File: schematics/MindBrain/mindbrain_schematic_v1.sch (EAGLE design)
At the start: 42 parts, among them IC1 TL084P, IC2 TL084P

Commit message: created board files in Eagle, started layout
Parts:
- added C1, C2, C3, C4: (no value), SparkFun-Capacitors:CAPKIT
- added CON1: POWER, SparkFun-Connectors:M05X2SHD
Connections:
- new net N$25: CON1.3, CON1.4, CON1.5, CON1.6, CON1.7, CON1.8
- new net N$27: CON1.1, CON1.2
- new net N$28: CON1.10, CON1.9
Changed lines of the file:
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@@
 <part name="GND16" library="SparkFun-Aesthetics" deviceset="GND" device=""/>
 <part name="IC2" library="linear" deviceset="TL084" device="P"/>
+<part name="C1" library="SparkFun-Capacitors" deviceset="CAP" device="KIT"/>
+<part name="C2" library="SparkFun-Capacitors" deviceset="CAP" device="KIT"/>
+<part name="C3" library="SparkFun-Capacitors" deviceset="CAP" device="KIT"/>
+<part name="C4" library="SparkFun-Capacitors" deviceset="CAP" device="KIT"/>
+<part name="CON1" library="SparkFun-Connectors" deviceset="M05X2" device="SHD" value="POWER"/>
 </parts>
 <sheets>
@@
 <instance part="IC2" gate="C" x="88.9" y="7.62"/>
 <instance part="IC2" gate="D" x="88.9" y="-30.48"/>
+<instance part="C1" gate="G$1" x="-55.88" y="53.34"/>
+<instance part="C2" gate="G$1" x="-45.72" y="53.34"/>
+<instance part="C3" gate="G$1" x="-55.88" y="40.64"/>
+<instance part="C4" gate="G$1" x="-45.72" y="40.64"/>
+<instance part="CON1" gate="G$1" x="-45.72" y="81.28"/>
 </instances>
 <busses>
@@
 </segment>
 </net>
+<net name="N$25" class="0">
+<segment>
+<pinref part="CON1" gate="G$1" pin="3"/>
+<pinref part="CON1" gate="G$1" pin="5"/>
+<wire x1="-53.34" y1="83.82" x2="-53.34" y2="81.28" width="0.1524" layer="91"/>
+<pinref part="CON1" gate="G$1" pin="7"/>
+<wire x1="-53.34" y1="81.28" x2="-53.34" y2="78.74" width="0.1524" layer="91"/>
+<wire x1="-53.34" y1="81.28" x2="-58.42" y2="81.28" width="0.1524" layer="91"/>
+<wire x1="-58.42" y1="81.28" x2="-58.42" y2="96.52" width="0.1524" layer="91"/>
+<wire x1="-58.42" y1="96.52" x2="-33.02" y2="96.52" width="0.1524" layer="91"/>
+<wire x1="-33.02" y1="96.52" x2="-33.02" y2="81.28" width="0.1524" layer="91"/>
+<pinref part="CON1" gate="G$1" pin="4"/>
+<pinref part="CON1" gate="G$1" pin="6"/>
+<wire x1="-38.1" y1="83.82" x2="-38.1" y2="81.28" width="0.1524" layer="91"/>
+<pinref part="CON1" gate="G$1" pin="8"/>
+<wire x1="-38.1" y1="81.28" x2="-38.1" y2="78.74" width="0.1524" layer="91"/>
+<wire x1="-33.02" y1="81.28" x2="-38.1" y2="81.28" width="0.1524" layer="91"/>
+</segment>
+</net>
+<net name="N$27" class="0">
+<segment>
+<pinref part="CON1" gate="G$1" pin="1"/>
+<wire x1="-53.34" y1="86.36" x2="-55.88" y2="86.36" width="0.1524" layer="91"/>
+<wire x1="-55.88" y1="86.36" x2="-55.88" y2="93.98" width="0.1524" layer="91"/>
+<wire x1="-55.88" y1="93.98" x2="-35.56" y2="93.98" width="0.1524" layer="91"/>
+<wire x1="-35.56" y1="93.98" x2="-35.56" y2="86.36" width="0.1524" layer="91"/>
+<pinref part="CON1" gate="G$1" pin="2"/>
+<wire x1="-35.56" y1="86.36" x2="-38.1" y2="86.36" width="0.1524" layer="91"/>
+</segment>
+</net>
+<net name="N$28" class="0">
+<segment>
+<pinref part="CON1" gate="G$1" pin="9"/>
+<wire x1="-53.34" y1="76.2" x2="-55.88" y2="76.2" width="0.1524" layer="91"/>
+<wire x1="-55.88" y1="76.2" x2="-55.88" y2="68.58" width="0.1524" layer="91"/>
+<wire x1="-55.88" y1="68.58" x2="-35.56" y2="68.58" width="0.1524" layer="91"/>
+<wire x1="-35.56" y1="68.58" x2="-35.56" y2="76.2" width="0.1524" layer="91"/>
+<pinref part="CON1" gate="G$1" pin="10"/>
+<wire x1="-35.56" y1="76.2" x2="-38.1" y2="76.2" width="0.1524" layer="91"/>
+</segment>
+</net>

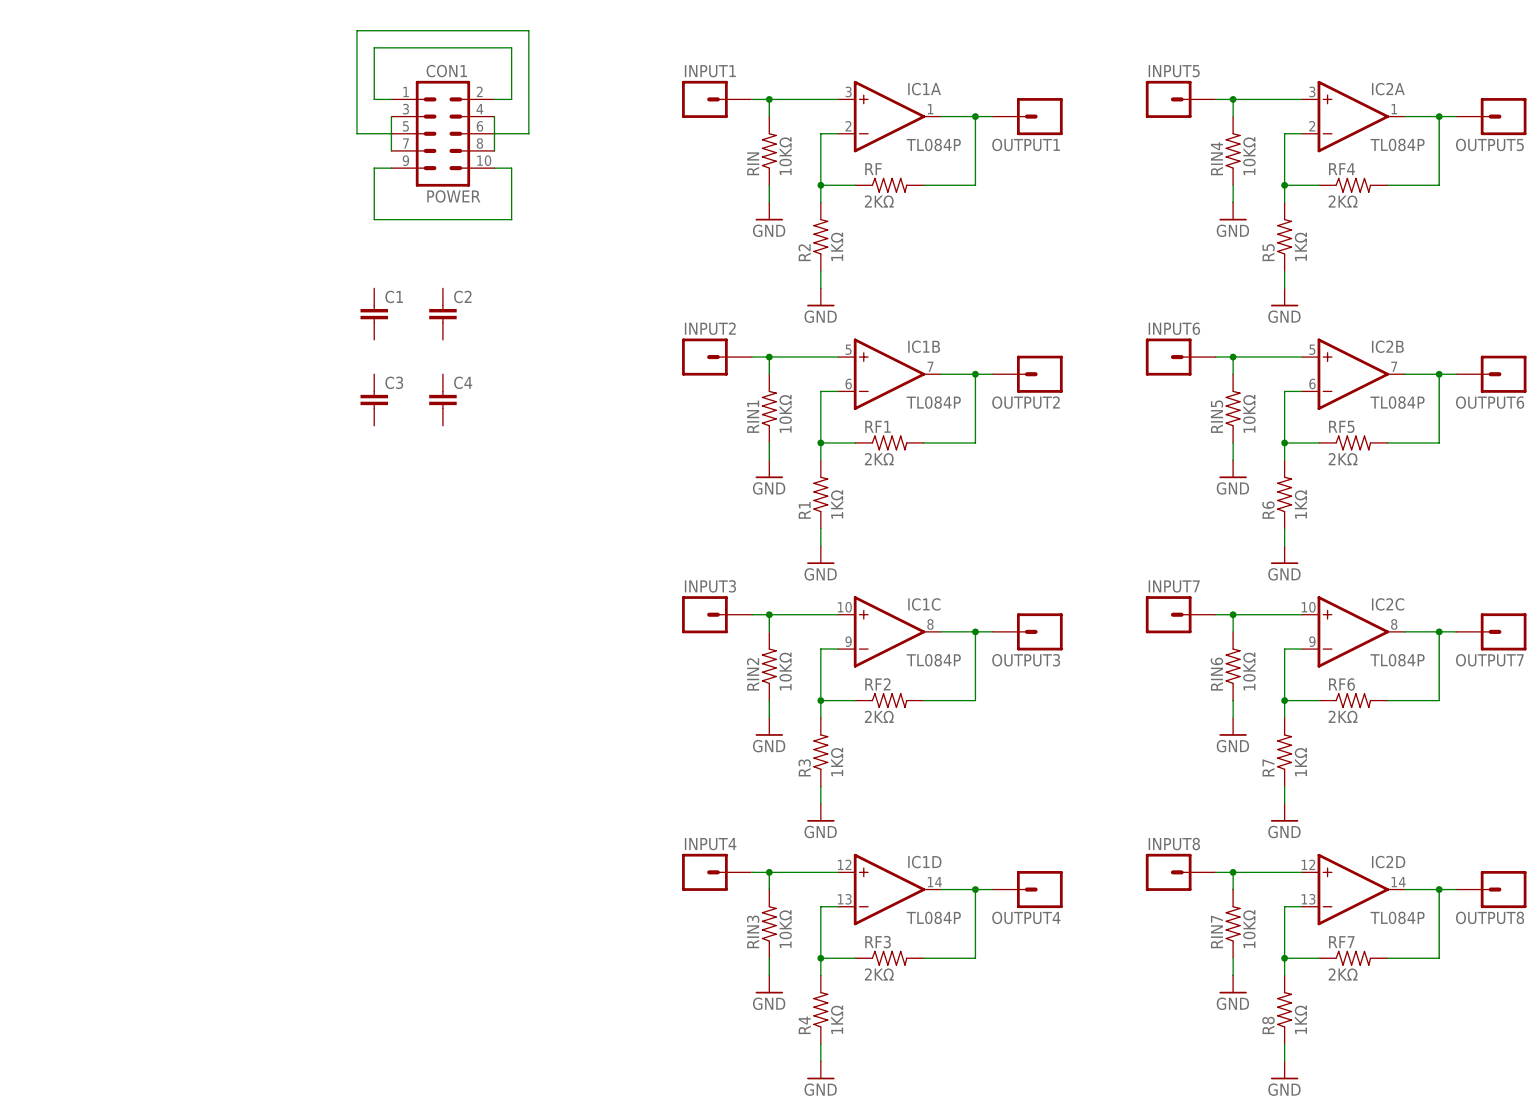
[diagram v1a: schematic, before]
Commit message: fixed component designator confusion
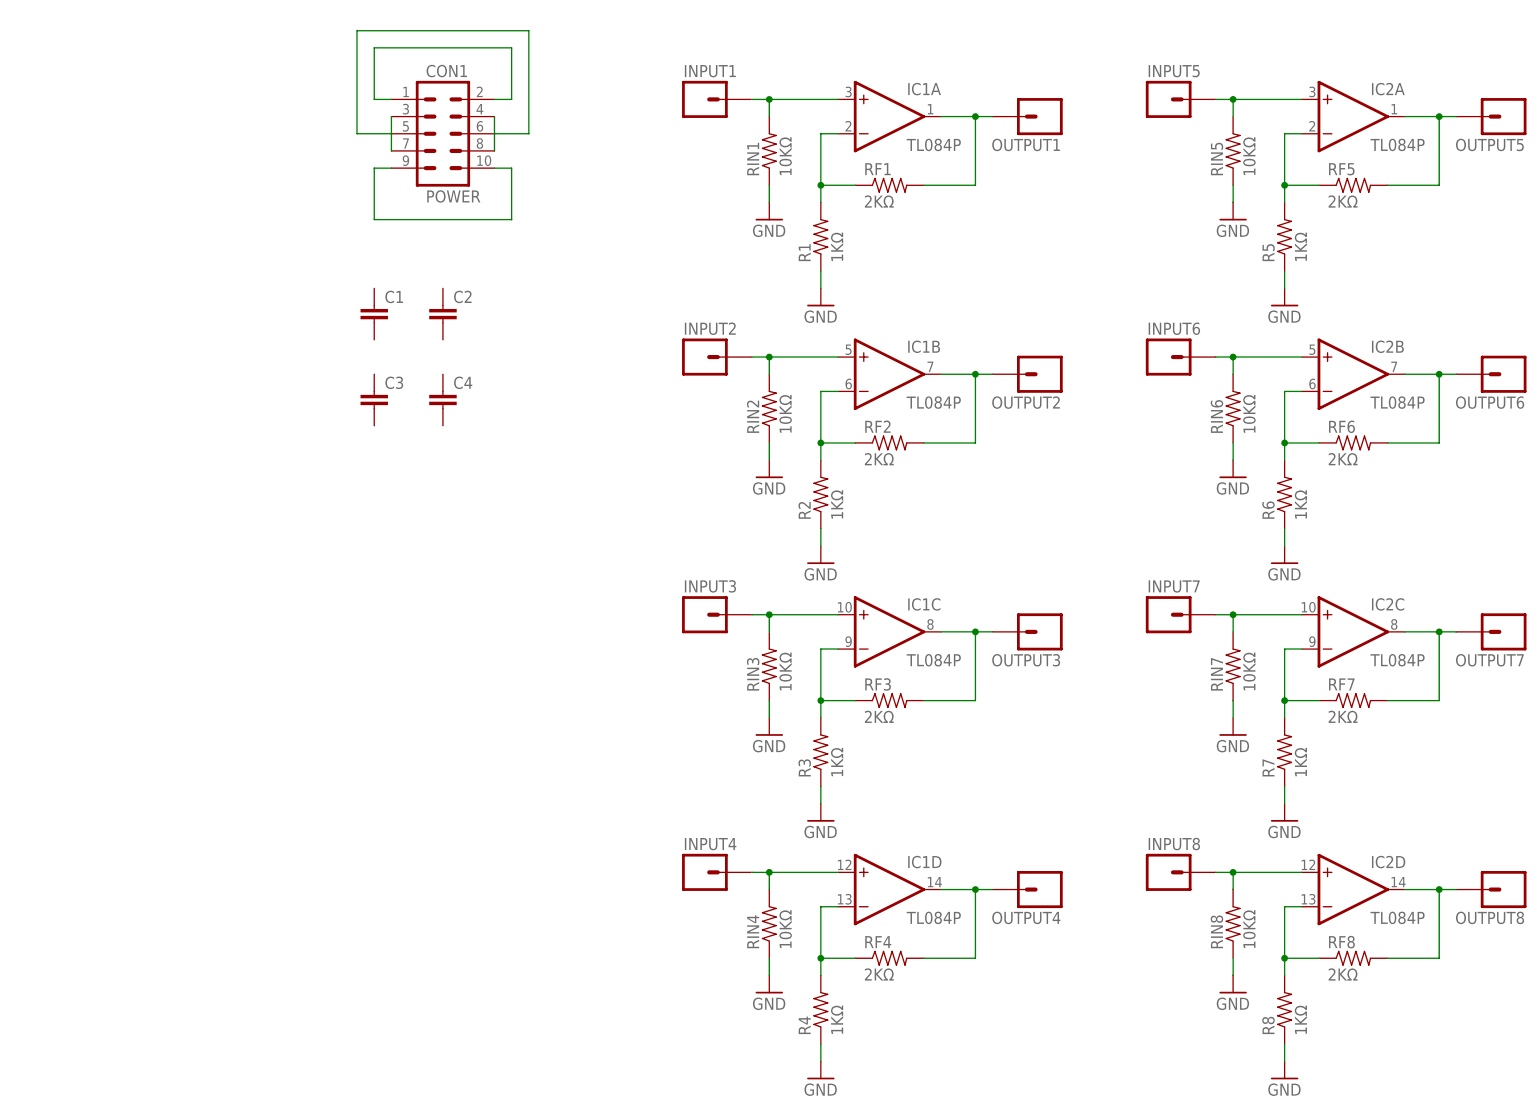
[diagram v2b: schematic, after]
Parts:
- removed RF: 2KΩ, SparkFun-Passives:RESISTORPTH-1/4W
- removed RIN: 10KΩ, SparkFun-Passives:RESISTORPTH-1/4W
- added RF8: 2KΩ, SparkFun-Passives:RESISTORPTH-1/4W
- added RIN8: 10KΩ, SparkFun-Passives:RESISTORPTH-1/4W
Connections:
- net GND: now also RIN8.1; no longer RIN.1
- net N$1: now also RIN1.2; no longer RIN.2
- net N$10: now also RIN4.2; no longer RIN3.2
- net N$11: now also RF4.2; no longer RF3.2
- net N$12: now also RF4.1; no longer RF3.1
- net N$13: now also RIN5.2; no longer RIN4.2
- net N$14: now also RF5.2; no longer RF4.2
- net N$15: now also RF5.1; no longer RF4.1
- net N$16: now also RIN6.2; no longer RIN5.2
- net N$17: now also RF6.2; no longer RF5.2
- net N$18: now also RF6.1; no longer RF5.1
- net N$19: now also RIN7.2; no longer RIN6.2
- net N$2: now also RF1.2; no longer RF.2
- net N$20: now also RF7.2; no longer RF6.2
- net N$21: now also RF7.1; no longer RF6.1
- net N$22: now also RIN8.2; no longer RIN7.2
- net N$23: now also RF8.2; no longer RF7.2
- net N$24: now also RF8.1; no longer RF7.1
- net N$3: now also R1.2, RF1.1; no longer R2.2, RF.1
- net N$4: now also RIN2.2; no longer RIN1.2
- net N$5: now also RF2.2; no longer RF1.2
- net N$6: now also R2.2, RF2.1; no longer R1.2, RF1.1
- net N$7: now also RIN3.2; no longer RIN2.2
- net N$8: now also RF3.2; no longer RF2.2
- net N$9: now also RF3.1; no longer RF2.1
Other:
- moved on the sheet: R1, R2, RF1, RF2, RF3, RF4, RF5, RF6, RF7, RIN1, RIN2, RIN3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

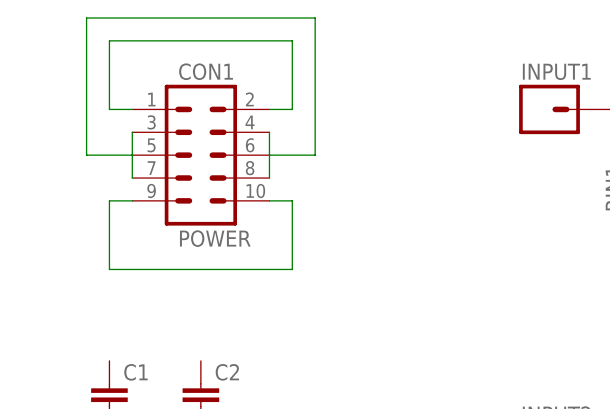
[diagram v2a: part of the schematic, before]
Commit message: connected power supply grounds to circuit ground
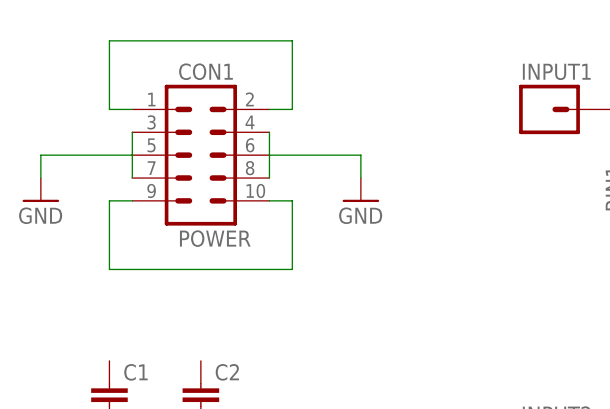
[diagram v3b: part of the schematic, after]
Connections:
- removed net N$25: CON1.3, CON1.4, CON1.5, CON1.6, CON1.7, CON1.8
- net GND: now also CON1.3, CON1.4, CON1.5, CON1.6, CON1.7, CON1.8
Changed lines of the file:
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@@
 <grid distance="0.1" unitdist="inch" unit="inch" style="lines" multiple="1" display="no" altdistance="0.01" altunitdist="inch" altunit="inch"/>
 <layers>
-<layer number="1" name="Top" color="4" fill="1" visible="no" active="no"/>
-<layer number="16" name="Bottom" color="1" fill="1" visible="no" active="no"/>
-<layer number="17" name="Pads" color="2" fill="1" visible="no" active="no"/>
-<layer number="18" name="Vias" color="2" fill="1" visible="no" active="no"/>
-<layer number="19" name="Unrouted" color="6" fill="1" visible="no" active="no"/>
-<layer number="20" name="Dimension" color="15" fill="1" visible="no" active="no"/>
-<layer number="21" name="tPlace" color="7" fill="1" visible="no" active="no"/>
-<layer number="22" name="bPlace" color="7" fill="1" visible="no" active="no"/>
-<layer number="23" name="tOrigins" color="15" fill="1" visible="no" active="no"/>
-<layer number="24" name="bOrigins" color="15" fill="1" visible="no" active="no"/>
-<layer number="25" name="tNames" color="7" fill="1" visible="no" active="no"/>
-<layer number="26" name="bNames" color="7" fill="1" visible="no" active="no"/>
-<layer number="27" name="tValues" color="7" fill="1" visible="no" active="no"/>
-<layer number="28" name="bValues" color="7" fill="1" visible="no" active="no"/>
+<layer number="1" name="Top" color="4" fill="1" visible="yes" active="no"/>
+<layer number="16" name="Bottom" color="1" fill="1" visible="yes" active="no"/>
+<layer number="17" name="Pads" color="2" fill="1" visible="yes" active="no"/>
+<layer number="18" name="Vias" color="2" fill="1" visible="yes" active="no"/>
+<layer number="19" name="Unrouted" color="6" fill="1" visible="yes" active="no"/>
+<layer number="20" name="Dimension" color="15" fill="1" visible="yes" active="no"/>
+<layer number="21" name="tPlace" color="7" fill="1" visible="yes" active="no"/>
+<layer number="22" name="bPlace" color="7" fill="1" visible="yes" active="no"/>
+<layer number="23" name="tOrigins" color="15" fill="1" visible="yes" active="no"/>
+<layer number="24" name="bOrigins" color="15" fill="1" visible="yes" active="no"/>
+<layer number="25" name="tNames" color="7" fill="1" visible="yes" active="no"/>
+<layer number="26" name="bNames" color="7" fill="1" visible="yes" active="no"/>
+<layer number="27" name="tValues" color="7" fill="1" visible="yes" active="no"/>
+<layer number="28" name="bValues" color="7" fill="1" visible="yes" active="no"/>
 <layer number="29" name="tStop" color="7" fill="3" visible="no" active="no"/>
 <layer number="30" name="bStop" color="7" fill="6" visible="no" active="no"/>
@@
 <layer number="35" name="tGlue" color="7" fill="4" visible="no" active="no"/>
 <layer number="36" name="bGlue" color="7" fill="5" visible="no" active="no"/>
-<layer number="37" name="tTest" color="7" fill="1" visible="no" active="no"/>
-<layer number="38" name="bTest" color="7" fill="1" visible="no" active="no"/>
+<layer number="37" name="tTest" color="7" fill="1" visible="yes" active="no"/>
+<layer number="38" name="bTest" color="7" fill="1" visible="yes" active="no"/>
 <layer number="39" name="tKeepout" color="4" fill="11" visible="no" active="no"/>
 <layer number="40" name="bKeepout" color="1" fill="11" visible="no" active="no"/>
@@
 <layer number="44" name="Drills" color="7" fill="1" visible="no" active="no"/>
 <layer number="45" name="Holes" color="7" fill="1" visible="no" active="no"/>
-<layer number="46" name="Milling" color="3" fill="1" visible="no" active="no"/>
-<layer number="47" name="Measures" color="7" fill="1" visible="no" active="no"/>
-<layer number="48" name="Document" color="7" fill="1" visible="no" active="no"/>
-<layer number="49" name="Reference" color="7" fill="1" visible="no" active="no"/>
-<layer number="50" name="dxf" color="7" fill="1" visible="no" active="no"/>
-<layer number="51" name="tDocu" color="6" fill="1" visible="no" active="no"/>
-<layer number="52" name="bDocu" color="7" fill="1" visible="no" active="no"/>
-<layer number="53" name="tGND_GNDA" color="7" fill="9" visible="no" active="no"/>
-<layer number="54" name="bGND_GNDA" color="1" fill="9" visible="no" active="no"/>
-<layer number="56" name="wert" color="7" fill="1" visible="no" active="no"/>
-<layer number="57" name="tCAD" color="7" fill="1" visible="no" active="no"/>
+<layer number="46" name="Milling" color="3" fill="1" visible="yes" active="no"/>
+<layer number="47" name="Measures" color="7" fill="1" visible="yes" active="no"/>
+<layer number="48" name="Document" color="7" fill="1" visible="yes" active="no"/>
+<layer number="49" name="Reference" color="7" fill="1" visible="yes" active="no"/>
+<layer number="50" name="dxf" color="7" fill="1" visible="yes" active="no"/>
+<layer number="51" name="tDocu" color="7" fill="1" visible="yes" active="no"/>
+<layer number="52" name="bDocu" color="7" fill="1" visible="yes" active="no"/>
+<layer number="53" name="tGND_GNDA" color="7" fill="9" visible="yes" active="no"/>
+<layer number="54" name="bGND_GNDA" color="1" fill="9" visible="yes" active="no"/>
+<layer number="56" name="wert" color="7" fill="1" visible="yes" active="no"/>
+<layer number="57" name="tCAD" color="7" fill="1" visible="yes" active="no"/>
 <layer number="90" name="Modules" color="5" fill="1" visible="yes" active="yes"/>
 <layer number="91" name="Nets" color="2" fill="1" visible="yes" active="yes"/>
@@
 <part name="C4" library="SparkFun-Capacitors" deviceset="CAP" device="KIT"/>
 <part name="CON1" library="SparkFun-Connectors" deviceset="M05X2" device="SHD" value="POWER"/>
+<part name="GND17" library="SparkFun-Aesthetics" deviceset="GND" device=""/>
+<part name="GND18" library="SparkFun-Aesthetics" deviceset="GND" device=""/>
 </parts>
 <sheets>
@@
 <instance part="C4" gate="G$1" x="-45.72" y="40.64"/>
 <instance part="CON1" gate="G$1" x="-45.72" y="81.28"/>
+<instance part="GND17" gate="1" x="-27.94" y="76.2"/>
+<instance part="GND18" gate="1" x="-63.5" y="76.2"/>
 </instances>
 <busses>
@@
 <pinref part="GND16" gate="1" pin="GND"/>
 <wire x1="78.74" y1="-53.34" x2="78.74" y2="-55.88" width="0.1524" layer="91"/>
+</segment>
+<segment>
+<pinref part="CON1" gate="G$1" pin="4"/>
+<pinref part="CON1" gate="G$1" pin="6"/>
+<wire x1="-38.1" y1="83.82" x2="-38.1" y2="81.28" width="0.1524" layer="91"/>
+<pinref part="CON1" gate="G$1" pin="8"/>
+<wire x1="-38.1" y1="81.28" x2="-38.1" y2="78.74" width="0.1524" layer="91"/>
+<pinref part="GND17" gate="1" pin="GND"/>
+<wire x1="-38.1" y1="81.28" x2="-27.94" y2="81.28" width="0.1524" layer="91"/>
+<wire x1="-27.94" y1="81.28" x2="-27.94" y2="78.74" width="0.1524" layer="91"/>
+</segment>
+<segment>
+<pinref part="CON1" gate="G$1" pin="7"/>
+<pinref part="CON1" gate="G$1" pin="5"/>
+<pinref part="CON1" gate="G$1" pin="3"/>
+<wire x1="-53.34" y1="83.82" x2="-53.34" y2="81.28" width="0.1524" layer="91"/>
+<wire x1="-53.34" y1="81.28" x2="-53.34" y2="78.74" width="0.1524" layer="91"/>
+<pinref part="GND18" gate="1" pin="GND"/>
+<wire x1="-53.34" y1="81.28" x2="-63.5" y2="81.28" width="0.1524" layer="91"/>
+<wire x1="-63.5" y1="81.28" x2="-63.5" y2="78.74" width="0.1524" layer="91"/>
 </segment>
 </net>
@@
 </segment>
 </net>
-<net name="N$25" class="0">
-<segment>
-<pinref part="CON1" gate="G$1" pin="3"/>
-<pinref part="CON1" gate="G$1" pin="5"/>
-<wire x1="-53.34" y1="83.82" x2="-53.34" y2="81.28" width="0.1524" layer="91"/>
-<pinref part="CON1" gate="G$1" pin="7"/>
-<wire x1="-53.34" y1="81.28" x2="-53.34" y2="78.74" width="0.1524" layer="91"/>
-<wire x1="-53.34" y1="81.28" x2="-58.42" y2="81.28" width="0.1524" layer="91"/>
-<wire x1="-58.42" y1="81.28" x2="-58.42" y2="96.52" width="0.1524" layer="91"/>
-<wire x1="-58.42" y1="96.52" x2="-33.02" y2="96.52" width="0.1524" layer="91"/>
-<wire x1="-33.02" y1="96.52" x2="-33.02" y2="81.28" width="0.1524" layer="91"/>
-<pinref part="CON1" gate="G$1" pin="4"/>
-<pinref part="CON1" gate="G$1" pin="6"/>
-<wire x1="-38.1" y1="83.82" x2="-38.1" y2="81.28" width="0.1524" layer="91"/>
-<pinref part="CON1" gate="G$1" pin="8"/>
-<wire x1="-38.1" y1="81.28" x2="-38.1" y2="78.74" width="0.1524" layer="91"/>
-<wire x1="-33.02" y1="81.28" x2="-38.1" y2="81.28" width="0.1524" layer="91"/>
-</segment>
-</net>
